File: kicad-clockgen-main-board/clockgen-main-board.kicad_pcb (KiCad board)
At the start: 2 copper layers, 70 x 64.4 mm, 15 parts, among them J1 CLK0_SMA, J2 CLK1_SMA, J3 Headswitch_SMA, J4 Headswitch_BNC

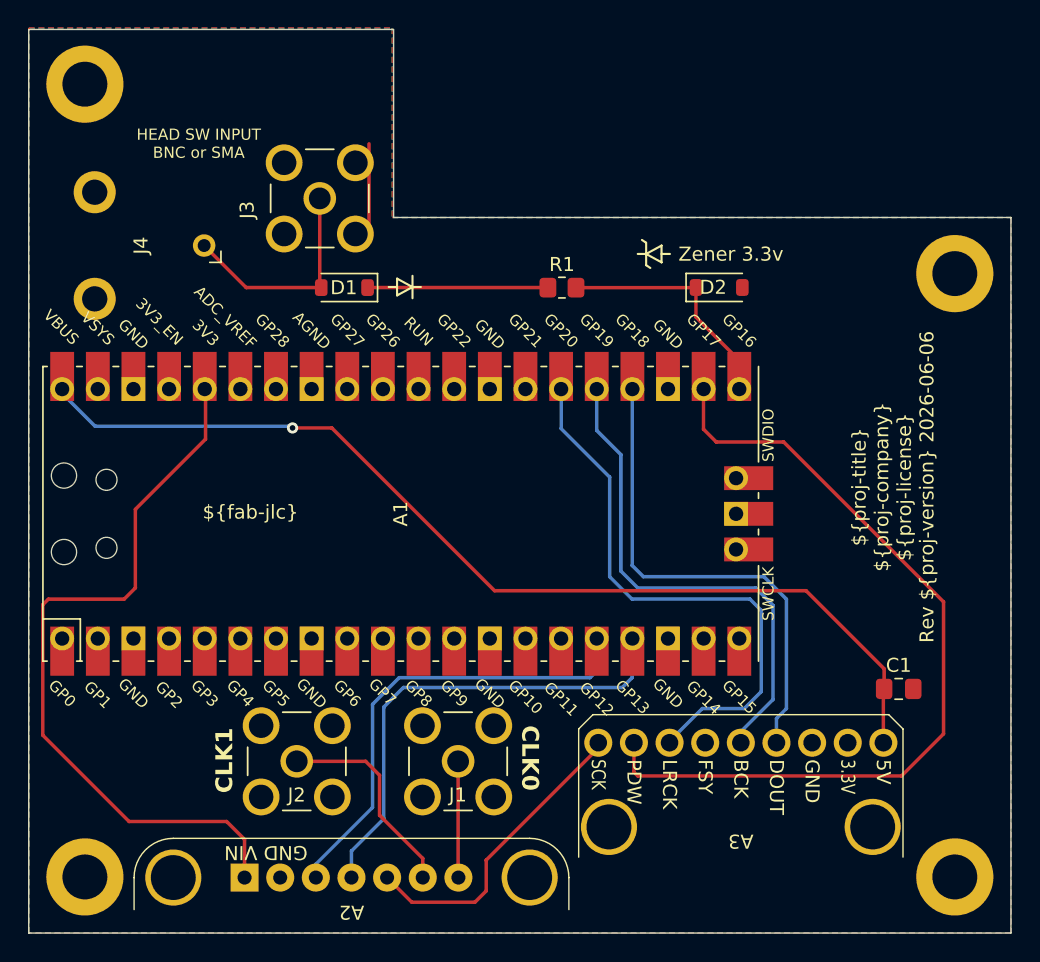
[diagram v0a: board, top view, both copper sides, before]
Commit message: Add initial fp-lib-table and sym-lib-table for KiCad project
- Created fp-lib-table with version 7 for footprint libraries.
- Created sym-lib-table with version 7 for symbol libraries.
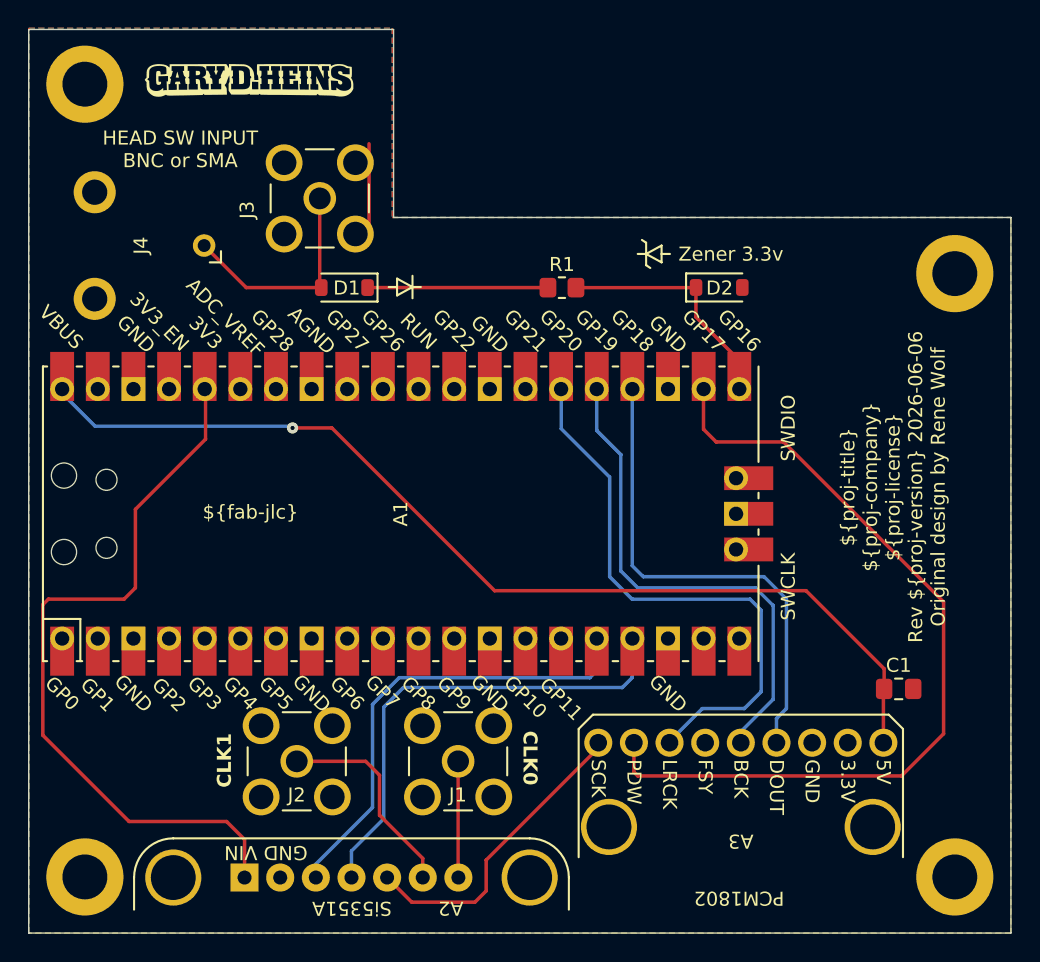
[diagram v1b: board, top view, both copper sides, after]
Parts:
- added G***: LOGO, GDH Graphics:16mm Straight GDH Wordmark, F.Cu at (113.7, 69.2)
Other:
- board text added: "${TITLE} ${COMPANY} ${proj-license} Rev ${REVISION} ${ISSUE_DATE} Original design by Rene Wolf"
- board text removed: "${TITLE} ${COMPANY} ${proj-license} Rev ${REVISION} ${ISSUE_DATE}"
